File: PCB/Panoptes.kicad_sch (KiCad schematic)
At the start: 114 parts, among them J1 Conn_01x02, J2 Conn_02x06_Odd_Even, J3 Conn_02x12_Odd_Even, J4 Conn_01x04, J5 Conn_01x02, J6 Conn_01x02, Q1 2N2222AUB, U1 SK0530, U2 SE555D, U3 ADS7882, U4 ARS14Y03, U5 OPA2350UA, U6 L79L05_SOT89, U7 OPA2350UA, U8 L78L33_SOT89, U9 L78L05_SOT89

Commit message: start of rev.3
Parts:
- removed J5: Conn_01x02, Connector_PinHeader_2.54mm:PinHeader_1x02_P2.54mm_Vertical, symbol Connector_Generic:Conn_01x02
- added J5: Conn_01x05, Connector_PinHeader_2.54mm:PinHeader_1x05_P2.54mm_Vertical, symbol Connector_Generic:Conn_01x05
- C14, C16, C18: footprint Capacitor_SMD:C_1206_3216Metric -> Capacitor_SMD:C_1812_4532Metric
- J6: now in the parts list
- renumbered TP12 to TP1, TP8 to TP10, TP4 to TP11, TP5 to TP12, TP9 to TP13, TP10 to TP2, TP13 to TP3, TP11 to TP4, TP6 to TP5, TP1 to TP6, TP2 to TP7, TP7 to TP8, TP3 to TP9
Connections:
- net +5V: now also J6.1 (Pin_1); no longer R2.1, U1.1 (Vcc)
- net +9V: now also J5.1 (Pin_1), J5.5 (Pin_5); no longer J6.1 (Pin_1)
- net -9V: now also J5.2 (Pin_2), J5.4 (Pin_4)
- net GND: now also J5.3 (Pin_3); no longer J6.2 (Pin_2)
- new net HV_+5V: J6.2 (Pin_2), R2.1, U1.1 (Vcc)

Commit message: All signals routed
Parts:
- removed C18: 200n, Capacitor_SMD:C_1812_4532Metric, symbol Device:C_Small
- removed H1, H2, H3, H4: MountingHole_Pad, MountingHole:MountingHole_4mm_Pad_Via, symbol Mechanical:MountingHole_Pad
- removed J2: Conn_02x06_Odd_Even, Connector_PinHeader_2.54mm:PinHeader_2x06_P2.54mm_Vertical, symbol Connector_Generic:Conn_02x06_Odd_Even
- removed J3: Conn_02x12_Odd_Even, Connector_PinHeader_2.54mm:PinHeader_2x12_P2.54mm_Vertical, symbol Connector_Generic:Conn_02x12_Odd_Even
- removed J4: Conn_01x04, Connector_PinHeader_2.54mm:PinHeader_1x04_P2.54mm_Vertical, symbol Connector_Generic:Conn_01x04
- removed J5: Conn_01x05, Connector_PinHeader_2.54mm:PinHeader_1x05_P2.54mm_Vertical, symbol Connector_Generic:Conn_01x05
- removed R13, R16, R2, R21, R24, R28, R3, R33, R8: 10k, Resistor_SMD:R_1206_3216Metric, symbol Device:R_Small
- removed R29, R31: 1k, Resistor_SMD:R_1206_3216Metric, symbol Device:R_Small
- removed TP4: HV, TestPoint:TestPoint_Pad_D1.0mm, symbol Connector:TestPoint
- removed U4: ARS14Y03, Panoptes:ARS14Y03, symbol Panoptes:ARS14Y03
- removed U5: OPA2350UA, Package_SO:SOIC-8_3.9x4.9mm_P1.27mm, symbol Panoptes:OPA2350UA
- added J1: Conn_02x05_Odd_Even, Connector_PinSocket_2.54mm:PinSocket_2x05_P2.54mm_Horizontal, symbol Connector_Generic:Conn_02x05_Odd_Even
- added J2: Conn_02x10_Odd_Even, Connector_PinSocket_2.54mm:PinSocket_2x10_P2.54mm_Horizontal, symbol Connector_Generic:Conn_02x10_Odd_Even
- added J3: Conn_01x02, Connector_PinSocket_2.54mm:PinSocket_1x02_P2.54mm_Horizontal, symbol Connector_Generic:Conn_01x02
- added J4: Conn_01x03, Panoptes:STX-3500-3NTR, symbol Connector_Generic:Conn_01x03
- added J5: Conn_01x03, Connector_PinHeader_2.54mm:PinHeader_1x03_P2.54mm_Vertical, symbol Connector_Generic:Conn_01x03
- added R27: 100, Resistor_SMD:R_1206_3216Metric, symbol Device:R_Small
- added RV1, RV4, RV5: 20k, Panoptes:Bourns 3361P, symbol Device:R_Potentiometer_Small
- added RV2, RV3: 2k, Panoptes:Bourns 3361P, symbol Device:R_Potentiometer_Small
- added RV6: 10k, Panoptes:Bourns 3361P, symbol Device:R_Potentiometer_Small
- added U6: OPA2350UA, Package_SO:SOIC-8_3.9x4.9mm_P1.27mm, symbol Panoptes:OPA2350UA
- added unit 2 of U7
- added unit 3 of U7
- C37: renamed from C14; footprint Capacitor_SMD:C_1812_4532Metric -> Capacitor_THT:C_Disc_D10.5mm_W5.0mm_P7.50mm; DK_Detail_Page https://www.digikey.com/en/products/detail/kemet/C1812X204K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 -> https://www.digikey.com/en/products/detail/tdk-corporation/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; DK_PN 399-C1812X204KDRLCAUTOCT-ND -> 445-181041-ND; MPN C1812X204KDRLCAUTO -> CK45-B3FD221KYGNA; Manufacturer KEMET -> TDK Corporation
- C38: renamed from C16; footprint Capacitor_SMD:C_1812_4532Metric -> Capacitor_THT:C_Disc_D10.5mm_W5.0mm_P7.50mm; DK_Detail_Page https://www.digikey.com/en/products/detail/kemet/C1812X204K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 -> https://www.digikey.com/en/products/detail/tdk-corporation/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; DK_PN 399-C1812X204KDRLCAUTOCT-ND -> 445-181041-ND; MPN C1812X204KDRLCAUTO -> CK45-B3FD221KYGNA; Manufacturer KEMET -> TDK Corporation
- J6: renamed from J1; DK_Detail_Page (none) -> n/a; DK_PN (none) -> n/a; MPN (none) -> n/a; Manufacturer (none) -> n/a
- Q1: value 2N2222AUB -> MMBT3904; footprint Panoptes:2N2222AUB -> Package_TO_SOT_SMD:SOT-23-3; DK_Detail_Page https://www.digikey.com/en/products/detail/microchip-techno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 -> https://www.digikey.com/en/products/detail/micro-commercial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; DK_PN 2N2222AUBMS-ND -> MMBT3904TPMSCT-ND; MPN 2N2222AUB -> MMBT3904-TP; Manufacturer Microchip Technology -> Micro Commercial Co
- TP1: renamed from TP3; value Pulse out -> P_out; DK_Detail_Page (none) -> n/a; DK_PN (none) -> n/a; MPN (none) -> n/a; Manufacturer (none) -> n/a
- TP10: renamed from TP7; value Amp2 Out -> A2_Out; DK_Detail_Page (none) -> n/a; DK_PN (none) -> n/a; MPN (none) -> n/a; Manufacturer (none) -> n/a
- TP11: renamed from TP2; value HV prog -> HV_prog; DK_Detail_Page (none) -> n/a; DK_PN (none) -> n/a; MPN (none) -> n/a; Manufacturer (none) -> n/a
- TP12: DK_Detail_Page (none) -> n/a; DK_PN (none) -> n/a; MPN (none) -> n/a; Manufacturer (none) -> n/a
- TP2: renamed from TP1; value Pulse Trig -> P_Trig; DK_Detail_Page (none) -> n/a; DK_PN (none) -> n/a; MPN (none) -> n/a; Manufacturer (none) -> n/a
- TP3: renamed from TP8; DK_Detail_Page (none) -> n/a; DK_PN (none) -> n/a; MPN (none) -> n/a; Manufacturer (none) -> n/a
- TP4: renamed from TP10; DK_Detail_Page (none) -> n/a; DK_PN (none) -> n/a; MPN (none) -> n/a; Manufacturer (none) -> n/a
- TP5: renamed from TP13; DK_Detail_Page (none) -> n/a; DK_PN (none) -> n/a; MPN (none) -> n/a; Manufacturer (none) -> n/a
- TP6: value Amp1 Out -> A1_Out; DK_Detail_Page (none) -> n/a; DK_PN (none) -> n/a; MPN (none) -> n/a; Manufacturer (none) -> n/a
- TP7: renamed from TP9; value Amp3 Out -> A3_Out; DK_Detail_Page (none) -> n/a; DK_PN (none) -> n/a; MPN (none) -> n/a; Manufacturer (none) -> n/a
- TP8: renamed from TP5; value Test Pulse -> Test_P; DK_Detail_Page (none) -> n/a; DK_PN (none) -> n/a; MPN (none) -> n/a; Manufacturer (none) -> n/a
- TP9: renamed from TP11; DK_Detail_Page (none) -> n/a; DK_PN (none) -> n/a; MPN (none) -> n/a; Manufacturer (none) -> n/a
- U7: DK_Detail_Page https://www.digikey.com/en/products/detail/texas-instruments/OPA2350UA/275846 -> https://www.digikey.com/en/products/detail/texas-instruments/OPA2350UA-2K5/301204; DK_PN OPA2350UA-ND -> 296-26258-1-ND; MPN OPA2350UA -> OPA2350UA/2K5
- renumbered C5 to C1, C3 to C10, C6 to C11, C10 to C12, C15 to C14, C17 to C15, C19 to C16, C7 to C17, C11 to C18, C25 to C19, C9 to C2, C28 to C20, C30 to C21, C2 to C22, C4 to C23, C8 to C24, C12 to C25, C32 to C26, C34 to C27, C37 to C28, C39 to C29, C20 to C3, C40 to C30, C41 to C31, C21 to C32, C23 to C33, C26 to C34, C38 to C35, C22 to C4, C33 to C40, C35 to C41, C24 to C5, C27 to C6, C29 to C7, C31 to C8, C1 to C9, J6 to J7, R9 to R1, R12 to R10, R19 to R11, R14 to R12, R1 to R13, R30 to R14, R34 to R15, R37 to R16, R22 to R17, R20 to R18, R25 to R19, R15 to R2, R23 to R20, R32 to R21, R35 to R22, R36 to R23, R27 to R24, R6 to R25, R10 to R3, R17 to R4, R4 to R5, R5 to R6, R11 to R7, R7 to R8, R18 to R9, U2 to U1, U3 to U2, U6 to U3, U8 to U4, U9 to U5, U1 to U8
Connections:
- net +5V: now also U6.8 (V+), U7.8 (V+); no longer U7.8 (V+)
- net +9V: now also J4.2 (Pin_2)
- net -5V: now also U6.4 (V-), U7.4 (V-); no longer U7.4 (V-)
- net -9V: now also J4.1 (Pin_1)
- net A_out_1: now also U7.1
- net A_out_3: now also RV2.3, RV4.1, U6.1; no longer U7.1 (A_out)
- net B-2: now also RV1.2, U7.6 (B-); no longer R26.2
- net BUSY: now also J1.2 (Pin_2)
- net B_out_2: now also RV1.3, U6.3 (A+), U7.7; no longer R26.1, U7.3 (A+)
- net B_out_4: now also C35.1, C36.1, U6.7; no longer C35.2, C36.2, U7.7 (B_out)
- net COM: now also U7.2 (A-), J5.2 (Pin_2)
- net DB0: now also J2.17 (Pin_17)
- net DB1: now also J2.15 (Pin_15)
- net DB10: now also J2.6 (Pin_6)
- net DB11: now also J2.4 (Pin_4)
- net DB2: now also J2.11 (Pin_11)
- net DB3: now also J2.9 (Pin_9)
- net DB4: now also J2.5 (Pin_5)
- net DB5: now also J2.3 (Pin_3)
- net DB6: now also J2.18 (Pin_18)
- net DB7: now also J2.16 (Pin_16)
- net DB8: now also J2.12 (Pin_12)
- net DB9: now also J2.10 (Pin_10)
- net GND: now also U7.3 (A+), J1.3 (Pin_3), J1.4 (Pin_4), J1.7 (Pin_7), J1.8 (Pin_8), J2.1 (Pin_1), J2.13 (Pin_13), J2.14 (Pin_14), J2.19 (Pin_19), J2.2 (Pin_2), J2.20 (Pin_20), J2.7 (Pin_7), J2.8 (Pin_8), J3.2 (Pin_2), J4.3 (Pin_3), R27.1, RV5.3, U7.5 (B+)
- net HV_+5V: now also R26.1
- net NC: now also C38.2, J5.3 (Pin_3)
- net NO: now also J5.1 (Pin_1)
- net TR: now also J3.1 (Pin_1)
- net Vprogram: now also R26.2, RV6.1
- net ~A_PWD: now also J1.6 (Pin_6)
- net ~CONVST: now also J1.1 (Pin_1)
- net ~CS: now also J1.9 (Pin_9)
- net ~PWD_RST: now also J1.10 (Pin_10)
- net ~RD: now also J1.5 (Pin_5)
- net A-3: no longer names the net of R24.2
- net A-3: now also RV4.2, U6.2 (A-); no longer U7.2 (A-)
- net B+4: no longer names the net of C40.1, C41.1
- net B+4: now also RV3.1, U6.5 (B+); no longer U7.5 (B+)
- net B-4: no longer names the net of R21.1
- net B-4: now also RV5.2, U6.6 (B-); no longer U7.6 (B-)
- new net: C35.2, C36.2, RV2.2, RV3.2
- new net: R27.2, RV6.2
- no-connect marks 0 -> 5
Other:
- moved on the sheet: C10, C11, C12, C17, C18, C19, C20, C21, C22, C23, C24, C25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

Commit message: V3 completed
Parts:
- removed U6, U7: OPA2350UA, Package_SO:SOIC-8_3.9x4.9mm_P1.27mm, symbol Panoptes:OPA2350UA
- added H1: Enclosure, n/a, symbol Mechanical:MountingHole
- added R23, R24, R25: 500M, Resistor_THT:R_Axial_DIN0207_L6.3mm_D2.5mm_P7.62mm_Horizontal, symbol Device:R_Small
- added R29: 1k5, Resistor_SMD:R_1206_3216Metric, symbol Device:R_Small
- added R30: 1M5, Resistor_SMD:R_1206_3216Metric, symbol Device:R_Small
- added TP10: HV_measure, TestPoint:TestPoint_Pad_D1.0mm, symbol Connector:TestPoint
- added U6, U7: opa2727, Package_DFN_QFN:DFN-8-1EP_3x3mm_P0.65mm_EP1.55x2.4mm, symbol Panoptes:opa2727
- J1: DK_Detail_Page (none) -> https://www.digikey.com/en/products/detail/sullins-connecto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; DK_PN (none) -> S9202-ND; MPN (none) -> SFH11-PBPC-D05-RA-BK; Manufacturer (none) -> Sullins Connector Solutions
- J2: DK_Detail_Page (none) -> https://www.digikey.com/en/products/detail/sullins-connecto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; DK_PN (none) -> S9205-ND; MPN (none) -> SFH11-PBPC-D10-RA-BK; Manufacturer (none) -> Sullins Connector Solutions
- J4: renamed from J5; DK_Detail_Page (none) -> n/a; DK_PN (none) -> n/a; MPN (none) -> n/a; Manufacturer (none) -> n/a
- J5: renamed from J7; DK_Detail_Page (none) -> n/a; DK_PN (none) -> n/a; MPN (none) -> n/a; Manufacturer (none) -> n/a
- J6: renamed from J3; DK_Detail_Page (none) -> https://www.digikey.com/en/products/detail/sullins-connecto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; DK_PN (none) -> S5438-ND; MPN (none) -> PPTC021LGBN-RC; Manufacturer (none) -> Sullins Connector Solutions
- R1, R10, R2, R3, R7: DK_Detail_Page https://www.digikey.com/en/products/detail/stackpole-electronics-inc/RNCF1206BKE1M00/2027096 -> https://www.digikey.com/en/products/detail/stackpole-electronics-inc/RMCF1206FT1M00/1759703; DK_PN RNCF1206BKE1M00CT-ND -> RMCF1206FT1M00CT-ND; MPN RNCF1206BKE1M00 -> RMCF1206FT1M00
- R11, R13, R14, R15, R16, R19, R9: DK_Detail_Page https://www.digikey.com/en/products/detail/stackpole-electronics-inc/RNCS1206BKE1K00/1800333 -> https://www.digikey.com/en/products/detail/stackpole-electronics-inc/RMCF1206FT1K00/1759616; DK_PN RNCS1206BKE1K00CT-ND -> RMCF1206FT1K00CT-ND; MPN RNCS1206BKE1K00 -> RMCF1206FT1K00
- R12, R5, R6, R8: DK_Detail_Page https://www.digikey.com/en/products/detail/stackpole-electronichttps://www.digikey.com/en/products/detail/stackpole-electronics-inc/RNCS1206BKE10K0/1800330s-inc/RNCS1206BKE10K0/1800330 -> https://www.digikey.com/en/products/detail/stackpole-electronics-inc/RMCF1206FT10K0/1759669; DK_PN RNCS1206BKE10K0CT-ND -> RMCF1206FT10K0CT-ND; MPN RNCS1206BKE10K0 -> RMCF1206FT10K0
- R17, R18, R20: DK_Detail_Page https://www.digikey.com/en/products/detail/vishay-beyschlag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 -> https://www.digikey.com/en/products/detail/stackpole-electr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; DK_PN 749-MCA1206MD1005BP500CT-ND -> RMCF1206FT10M0CT-ND; MPN MCA1206MD1005BP500 -> RMCF1206FT10M0; Manufacturer Vishay Dale -> Stackpole Electronics Inc
- R21: renamed from R25; DK_Detail_Page https://www.digikey.com/en/products/detail/stackpole-electronichttps://www.digikey.com/en/products/detail/stackpole-electronics-inc/RNCS1206BKE10K0/1800330s-inc/RNCS1206BKE10K0/1800330 -> https://www.digikey.com/en/products/detail/stackpole-electronics-inc/RMCF1206FT10K0/1759669; DK_PN RNCS1206BKE10K0CT-ND -> RMCF1206FT10K0CT-ND; MPN RNCS1206BKE10K0 -> RMCF1206FT10K0
- R22: renamed from R26; DK_Detail_Page https://www.digikey.com/en/products/detail/stackpole-electronichttps://www.digikey.com/en/products/detail/stackpole-electronics-inc/RNCS1206BKE10K0/1800330s-inc/RNCS1206BKE10K0/1800330 -> https://www.digikey.com/en/products/detail/stackpole-electronics-inc/RMCF1206FT10K0/1759669; DK_PN RNCS1206BKE10K0CT-ND -> RMCF1206FT10K0CT-ND; MPN RNCS1206BKE10K0 -> RMCF1206FT10K0
- R26: renamed from R21; DK_Detail_Page https://www.digikey.com/en/products/detail/panasonic-electr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 -> https://www.digikey.com/en/products/detail/vishay-dale/CRCW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; DK_PN P5.9KBCCT-ND -> 541-5.90KFCT-ND; MPN ERA-8AEB5901V -> CRCW12065K90FKEA; Manufacturer Panasonic Electronic Components -> Vishay Dale
- R27: renamed from R22; DK_Detail_Page https://www.digikey.com/en/products/detail/stackpole-electronics-inc/RTAN1206BKE22R0/6602201 -> https://www.digikey.com/en/products/detail/stackpole-electronics-inc/RMCF1206FT22R0/1759698; DK_PN RTAN1206BKE22R0CT-ND -> RMCF1206FT22R0CT-ND; MPN RTAN1206BKE22R0 -> RMCF1206FT22R0
- R28: renamed from R23; DK_Detail_Page https://www.digikey.com/en/products/detail/stackpole-electronics-inc/RTAN1206BKE22R0/6602201 -> https://www.digikey.com/en/products/detail/stackpole-electronics-inc/RMCF1206FT22R0/1759698; DK_PN RTAN1206BKE22R0CT-ND -> RMCF1206FT22R0CT-ND; MPN RTAN1206BKE22R0 -> RMCF1206FT22R0
- R31: renamed from R24; DK_Detail_Page https://www.digikey.com/en/products/detail/stackpole-electronics-inc/RNCS1206BKE1K00/1800333 -> https://www.digikey.com/en/products/detail/stackpole-electronics-inc/RMCF1206FT1K00/1759616; DK_PN RNCS1206BKE1K00CT-ND -> RMCF1206FT1K00CT-ND; MPN RNCS1206BKE1K00 -> RMCF1206FT1K00
- R32: renamed from R27; DK_Detail_Page https://www.digikey.com/en/products/detail/yageo/RT1206DRE0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 -> https://www.digikey.com/en/products/detail/stackpole-electr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; DK_PN 311-2954-1-ND -> RMCF1206FG100RCT-ND; MPN RT1206DRE07100RL -> RMCF1206FG100R; Manufacturer YAGEO -> Stackpole Electronics Inc
- R4: DK_Detail_Page https://www.digikey.com/en/products/detail/panasonic-electr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 -> https://www.digikey.com/en/products/detail/stackpole-electr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; DK_PN P1.5KBCCT-ND -> RMCF1206FT1K50CT-ND; MPN ERA-8AEB152V -> RMCF1206FT1K50; Manufacturer Panasonic Electronic Components -> Stackpole Electronics Inc
- TP1, TP2, TP3, TP4, TP5, TP6, TP7, TP8, TP9: footprint TestPoint:TestPoint_Pad_D1.0mm -> Connector_PinHeader_2.54mm:PinHeader_1x01_P2.54mm_Vertical
- TP12: renamed from TP10; footprint TestPoint:TestPoint_Pad_D1.0mm -> Connector_PinHeader_2.54mm:PinHeader_1x01_P2.54mm_Vertical
- TP13: renamed from TP12; footprint TestPoint:TestPoint_Pad_D1.0mm -> Connector_PinHeader_2.54mm:PinHeader_1x01_P2.54mm_Vertical
- renumbered C9 to C1, C4 to C10, C5 to C11, C6 to C12, C7 to C13, C8 to C14, C19 to C15, C20 to C16, C21 to C17, C13 to C18, C22 to C19, C10 to C2, C23 to C20, C24 to C21, C25 to C22, C14 to C23, C15 to C24, C16 to C25, C11 to C3, C37 to C36, C38 to C37, C36 to C38, C40 to C39, C12 to C4, C41 to C40, C1 to C5, C2 to C6, C17 to C7, C18 to C8, C3 to C9, J6 to J3, J4 to J7, RV6 to RV5, RV5 to RV6
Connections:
- net +5V: now also U6.8 (V+), U7.8 (V+)
- net -5V: now also U6.4 (V-), U7.4 (V-)
- net A_out_1: now also U6.1
- net A_out_3: now also U7.1
- net B-2: now also U6.6 (B-)
- net B_out_2: now also U6.7, U7.3 (A+)
- net B_out_4: now also U7.7
- net COM: now also U6.2 (A-)
- net GND: now also R29.1, U6.3 (A+), U6.5 (B+)
- net HV: now also R23.1
- net at C39.1, C40.1, RV3.1: now also U7.5 (B+)
- net at R31.2, RV4.2: now also U7.2 (A-)
- net at R26.1, RV6.2: now also U7.6 (B-)
- new net: R24.2, R25.1
- new net: R25.2, R30.2, TP10.1
- new net: R29.2, R30.1
- new net: R23.2, R24.1
- no-connect marks 5 -> 6
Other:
- note added: "A2D and Output Pins"
- note added: "Amplifier and Signal Conditioning"
- note added: "DRC Violation Avoidance Zone"
- note added: "HV Source"
- note added: "Misc. Power and Connectors"
- note added: "Test Pusle Generator"
- note added: "Voltage Regulators"
- company: (none) -> J. Jackson
- title: (none) -> Panoptes Analog Board Schematic
- moved on the sheet: C1, C10, C11, C12, C13, C14, C15, C16, C17, C18, C19, C2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

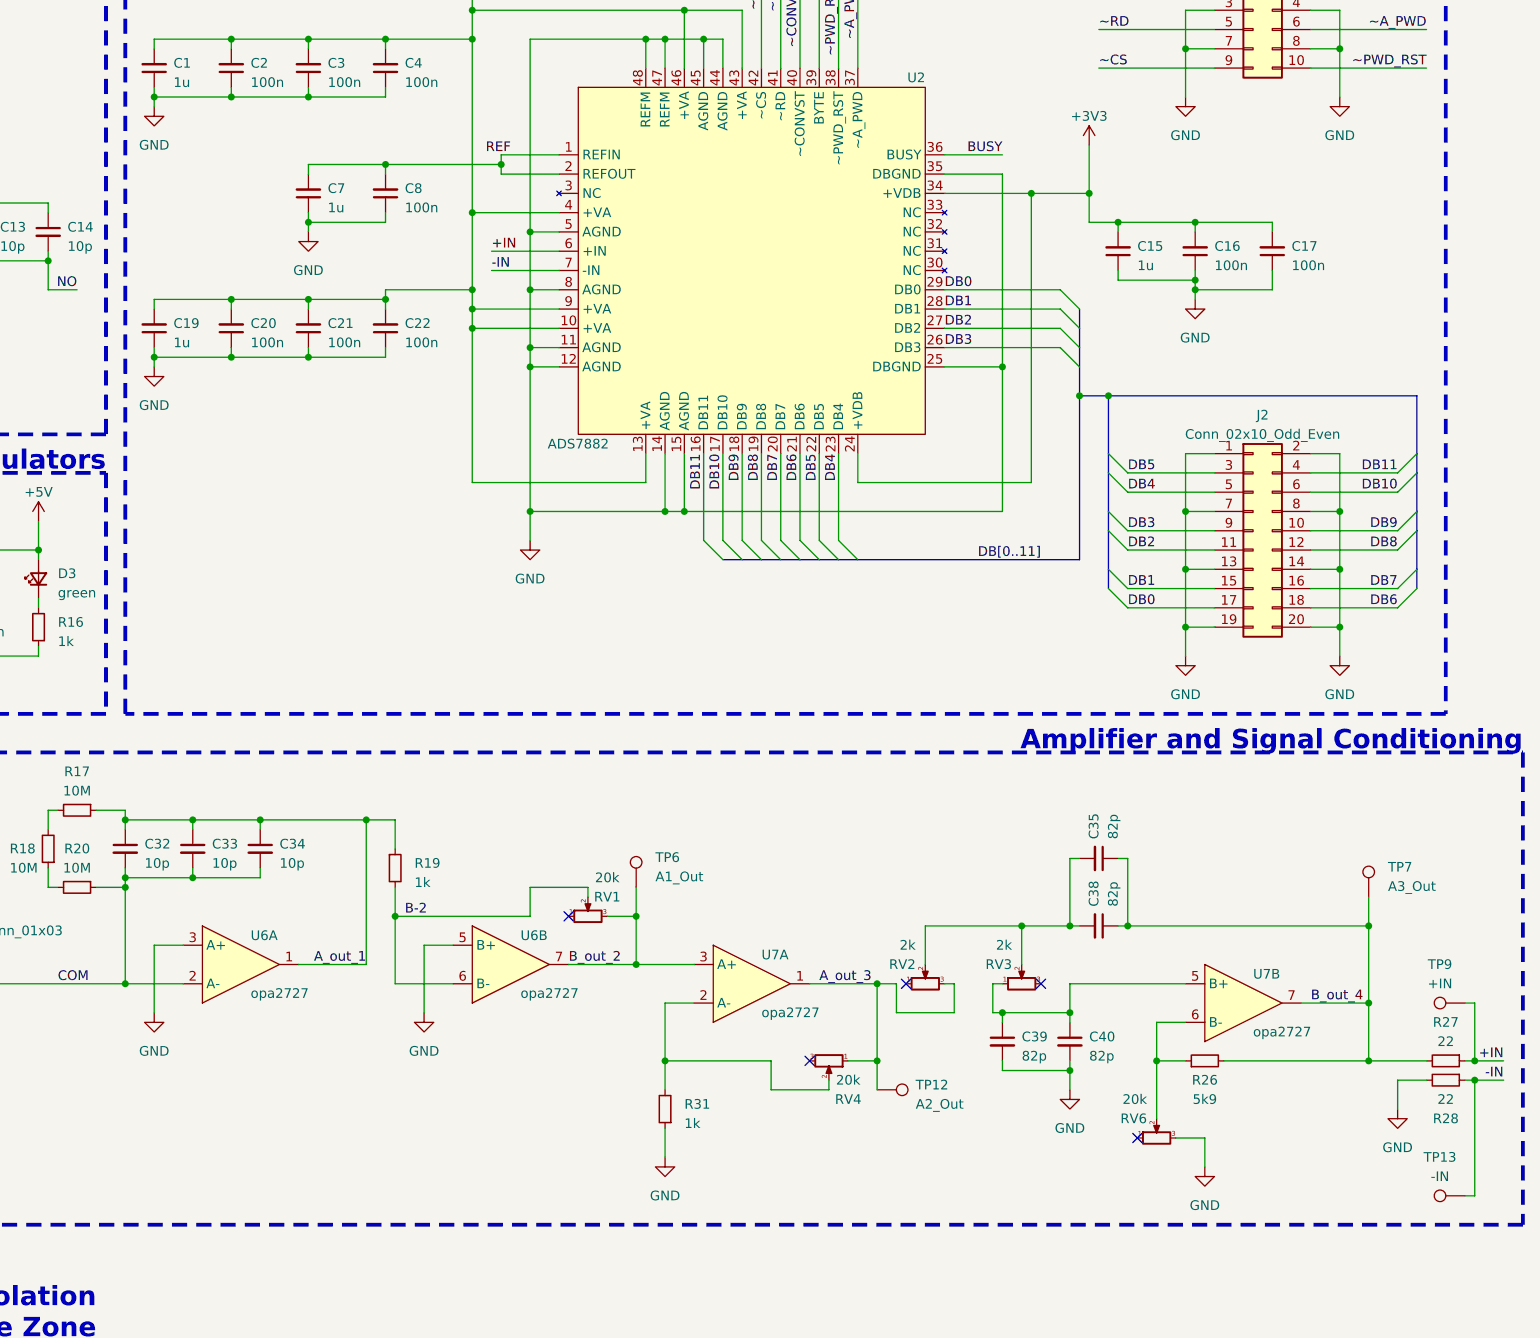
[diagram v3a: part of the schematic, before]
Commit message: Added DNP cap to ADC input.
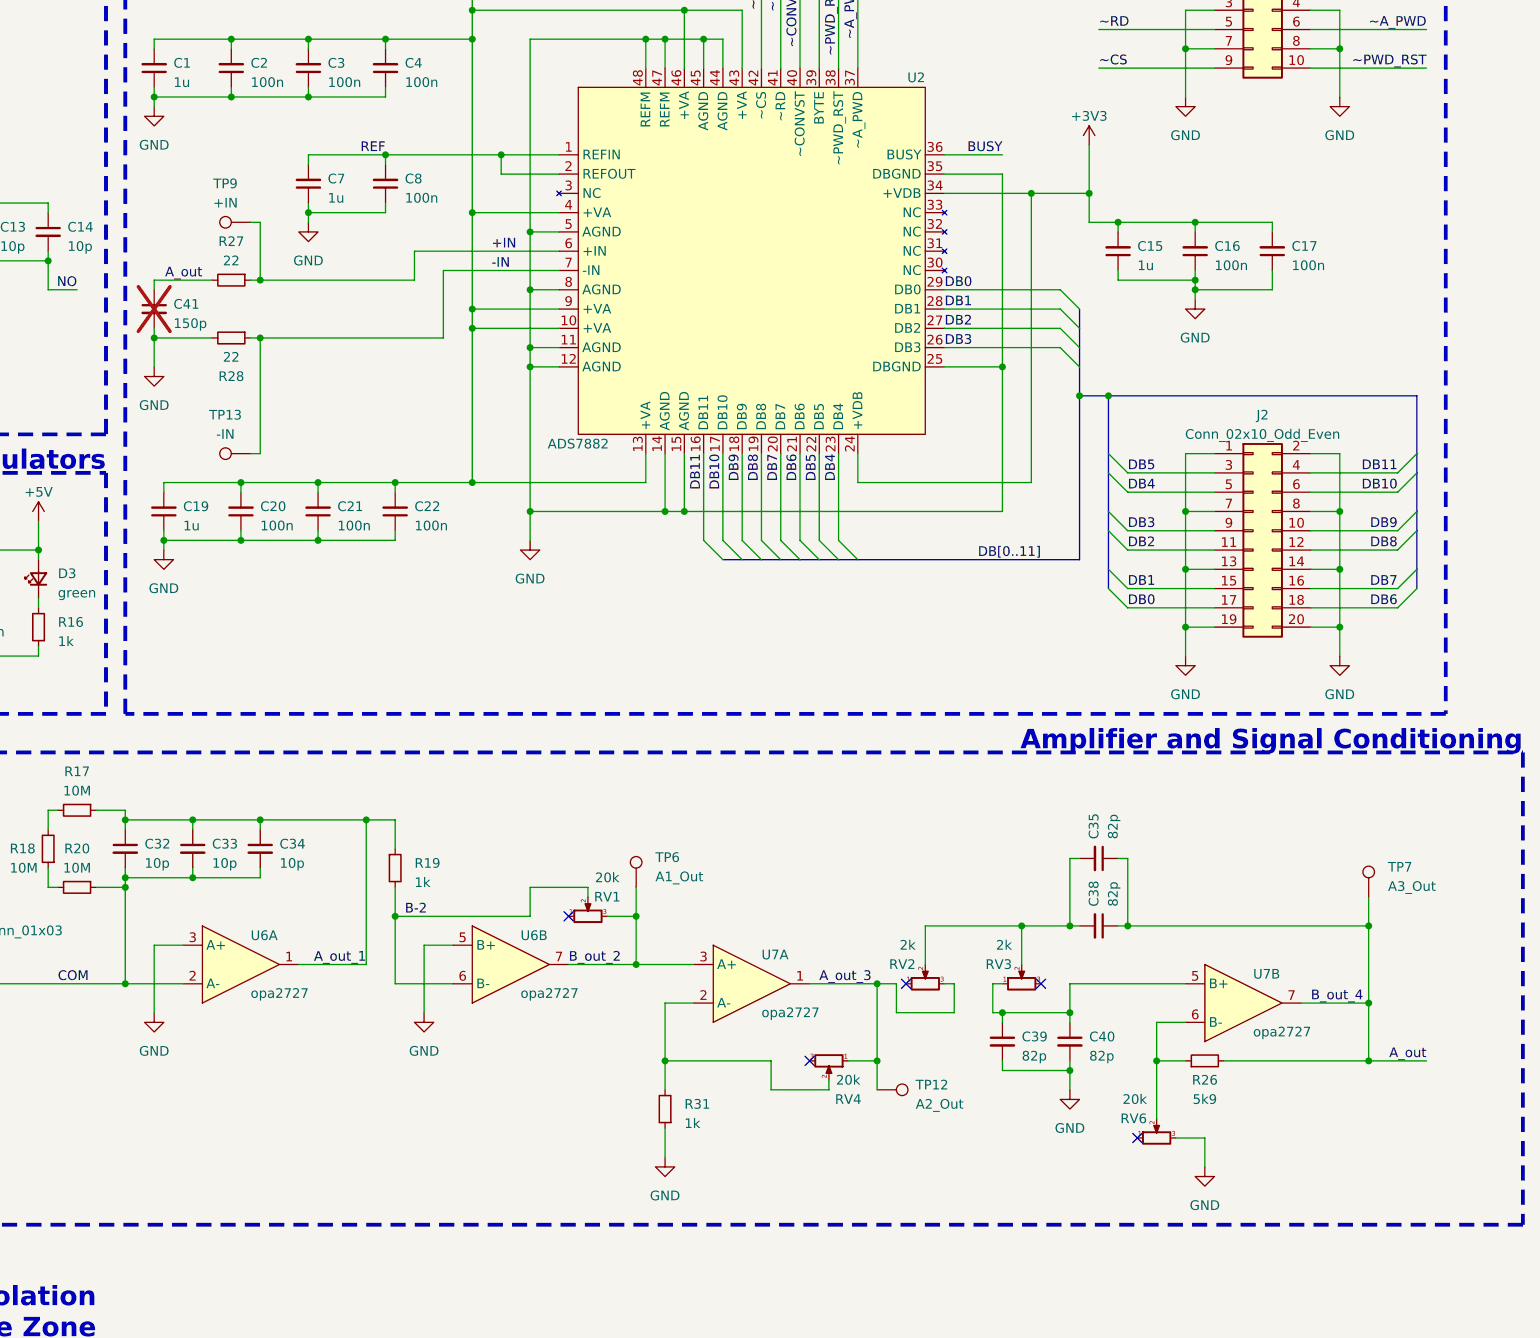
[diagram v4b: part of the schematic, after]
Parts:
- added C41: 150p, Capacitor_SMD:C_0603_1608Metric, symbol Device:C_Small
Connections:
- net GND: now also C41.2
- net B_out_4 renamed A_out
- net A_out: now also C41.1
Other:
- moved on the sheet: C19, C20, C21, C22, C7, C8, R27, R28, TP13, TP9
